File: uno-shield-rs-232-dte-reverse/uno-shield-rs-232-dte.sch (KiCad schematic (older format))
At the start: 19 parts, among them J1 Ctrl Route, J3 DSR/CTS, J4 DB9_Male, P1 Power, P2 Analog, P3 Digital, P4 Digital, P5 CONN_01X01, P7 CONN_01X01, U1 MAX232

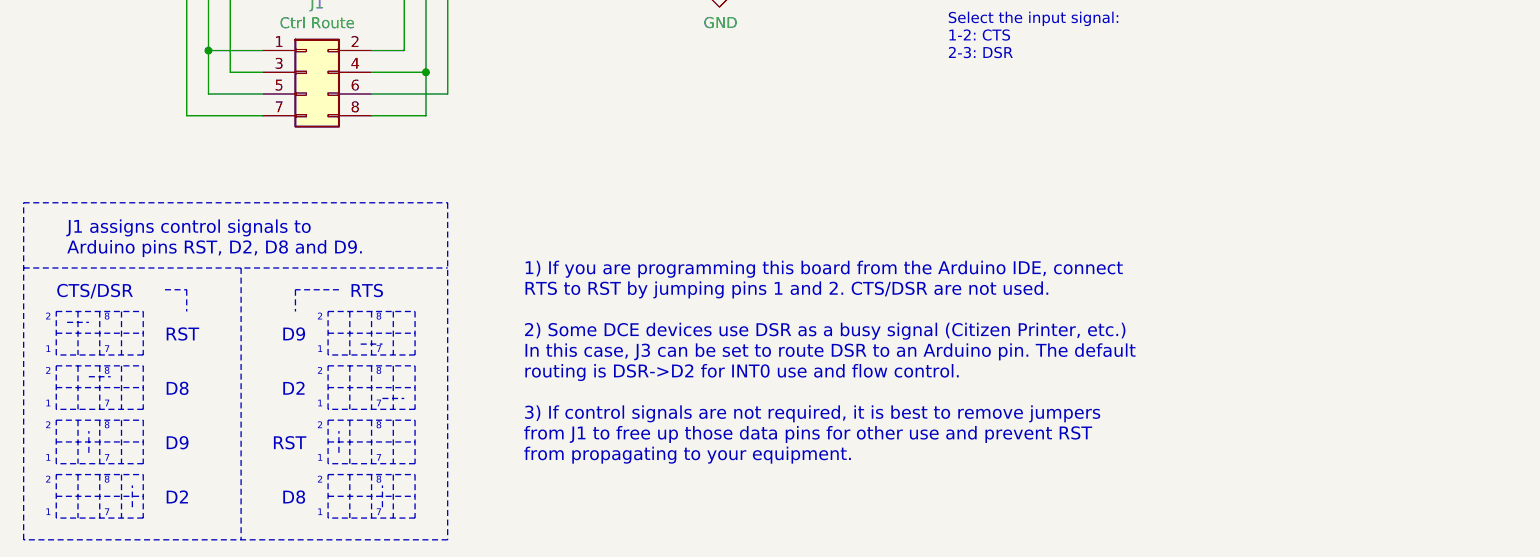
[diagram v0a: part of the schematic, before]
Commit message: Add DTE-Reverse
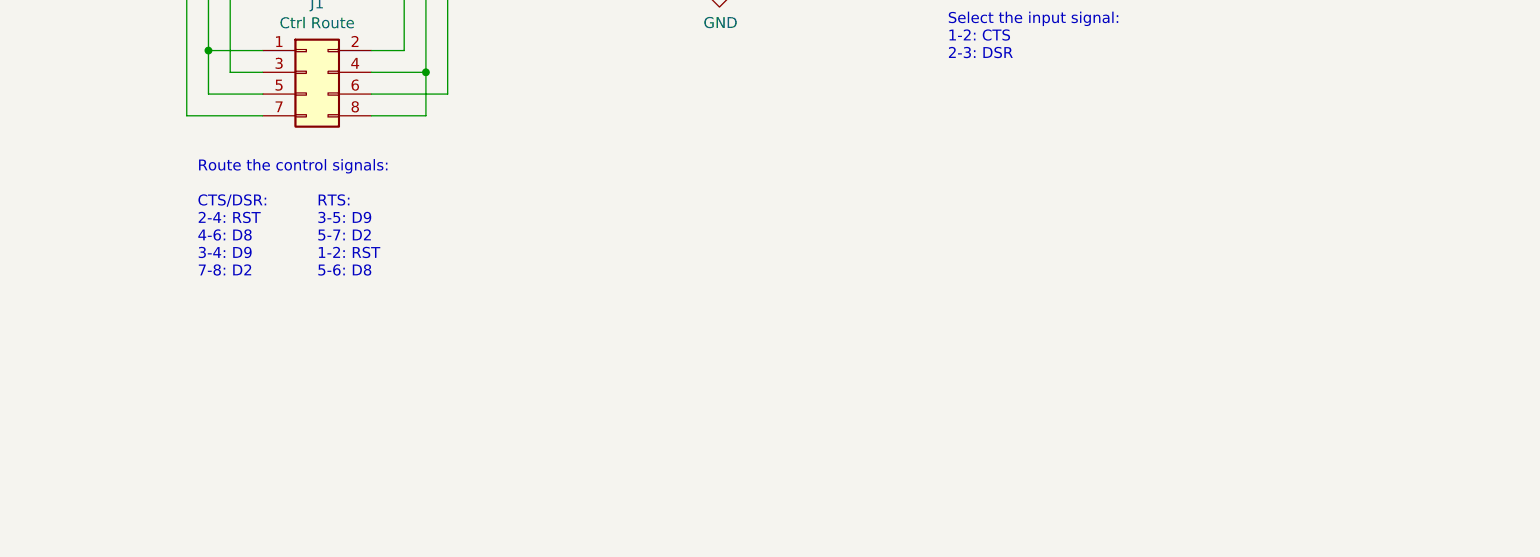
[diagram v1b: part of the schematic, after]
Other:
- note added: "RTS:\n3-5: D9\n5-7: D2\n1-2: RST\n5-6: D8"
- note added: "Route the control signals:\n\nCTS/DSR:\n2-4: RST\n4-6: D8\n3-4: D9\n7-8: D2"
- note removed: "1) If you are programming this board from the Arduino IDE, connect\nRTS to RST by jumping pins 1 and 2. CTS/DSR are not used.\n\n2) Some DCE devices use DSR as a busy signal (Citizen Printer, etc.)\nIn this case, J3 can be set to route DSR to an Arduino pin. The default\nrouting is DSR->D2 for INT0 use and flow control.\n\n3) If control signals are not required, it is best to remove jumpers\nfrom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"
- note removed: "2 8\n\n\n1 7"
- note removed: "CTS/DSR"
- note removed: "D2"
- note removed: "D8"
- note removed: "D9"
- note removed: "J1 assigns control signals to\nArduino pins RST, D2, D8 and D9."
- note removed: "RST"
- note removed: "RTS"
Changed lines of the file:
@@
 EESchema Schematic File Version 4
-LIBS:uno-shield-rs-232-dte-cache
+LIBS:uno-shield-rs-232-dce-cache
 EELAYER 30 0
 EELAYER END
@@
 NoConn ~ 9450 2700
 NoConn ~ 9450 2800
-Wire Notes Line
-	1100 5100 1500 5100
-Wire Notes Line
-	1500 5100 1500 5300
-Wire Notes Line
-	1500 5300 1100 5300
-Wire Notes Line
-	1100 5300 1100 5100
-Wire Notes Line
-	1200 5100 1200 5300
-Wire Notes Line
-	1300 5100 1300 5300
-Wire Notes Line
-	1400 5100 1400 5300
-Wire Notes Line
-	1100 5200 1500 5200
-Wire Notes Line
-	1100 5350 1500 5350
-Wire Notes Line
-	1500 5350 1500 5550
-Wire Notes Line
-	1500 5550 1100 5550
-Wire Notes Line
-	1100 5550 1100 5350
-Wire Notes Line
-	1200 5350 1200 5550
-Wire Notes Line
-	1300 5350 1300 5550
-Wire Notes Line
-	1400 5350 1400 5550
-Wire Notes Line
-	1100 5450 1500 5450
-Wire Notes Line
-	1100 5600 1500 5600
-Wire Notes Line
-	1500 5600 1500 5800
-Wire Notes Line
-	1500 5800 1100 5800
-Wire Notes Line
-	1100 5800 1100 5600
-Wire Notes Line
-	1200 5600 1200 5800
-Wire Notes Line
-	1300 5600 1300 5800
-Wire Notes Line
-	1400 5600 1400 5800
-Wire Notes Line
-	1100 5700 1500 5700
-Wire Notes Line
-	1100 5850 1500 5850
-Wire Notes Line
-	1500 5850 1500 6050
-Wire Notes Line
-	1500 6050 1100 6050
-Wire Notes Line
-	1100 6050 1100 5850
-Wire Notes Line
-	1200 5850 1200 6050
-Wire Notes Line
-	1300 5850 1300 6050
-Wire Notes Line
-	1400 5850 1400 6050
-Wire Notes Line
-	1100 5950 1500 5950
-Wire Notes Line
-	2350 5100 2750 5100
-Wire Notes Line
-	2750 5100 2750 5300
-Wire Notes Line
-	2750 5300 2350 5300
-Wire Notes Line
-	2350 5300 2350 5100
-Wire Notes Line
-	2450 5100 2450 5300
-Wire Notes Line
-	2550 5100 2550 5300
-Wire Notes Line
-	2650 5100 2650 5300
-Wire Notes Line
-	2350 5200 2750 5200
-Wire Notes Line
-	2350 5350 2750 5350
-Wire Notes Line
-	2750 5350 2750 5550
-Wire Notes Line
-	2750 5550 2350 5550
-Wire Notes Line
-	2350 5550 2350 5350
-Wire Notes Line
-	2450 5350 2450 5550
-Wire Notes Line
-	2550 5350 2550 5550
-Wire Notes Line
-	2650 5350 2650 5550
-Wire Notes Line
-	2350 5450 2750 5450
-Wire Notes Line
-	2350 5600 2750 5600
-Wire Notes Line
-	2750 5600 2750 5800
-Wire Notes Line
-	2750 5800 2350 5800
-Wire Notes Line
-	2350 5800 2350 5600
-Wire Notes Line
-	2450 5600 2450 5800
-Wire Notes Line
-	2550 5600 2550 5800
-Wire Notes Line
-	2650 5600 2650 5800
-Wire Notes Line
-	2350 5700 2750 5700
-Wire Notes Line
-	2350 5850 2750 5850
-Wire Notes Line
-	2750 5850 2750 6050
-Wire Notes Line
-	2750 6050 2350 6050
-Wire Notes Line
-	2350 6050 2350 5850
-Wire Notes Line
-	2450 5850 2450 6050
-Wire Notes Line
-	2550 5850 2550 6050
-Wire Notes Line
-	2650 5850 2650 6050
-Wire Notes Line
-	2350 5950 2750 5950
-Wire Notes Line width 100
-	1150 5150 1250 5150
-Wire Notes Line width 100
-	1250 5400 1350 5400
-Wire Notes Line width 100
-	1250 5750 1250 5650
-Wire Notes Line width 100
-	1450 6000 1450 5900
-Wire Notes Line width 100
-	2500 5250 2600 5250
-Wire Notes Line width 100
-	2600 5500 2700 5500
-Wire Notes Line width 100 style solid
-	2400 5750 2400 5650
-Wire Notes Line width 100
-	2600 6000 2600 5900
-Text Notes 1050 5300 0    31   ~ 0
-2                  8\n\n\n1                  7
-Text Notes 1050 5550 0    31   ~ 0
-2                  8\n\n\n1                  7
-Text Notes 1050 5800 0    31   ~ 0
-2                  8\n\n\n1                  7
-Text Notes 1050 6050 0    31   ~ 0
-2                  8\n\n\n1                  7
-Text Notes 2300 5300 0    31   ~ 0
-2                  8\n\n\n1                  7
-Text Notes 2300 5550 0    31   ~ 0
-2                  8\n\n\n1                  7
-Text Notes 2300 5800 0    31   ~ 0
-2                  8\n\n\n1                  7
-Text Notes 2300 6050 0    31   ~ 0
-2                  8\n\n\n1                  7
-Text Notes 1150 4850 0    59   ~ 0
-J1 assigns control signals to\nArduino pins RST, D2, D8 and D9.
-Text Notes 1100 5050 0    59   ~ 0
-CTS/DSR
-Text Notes 2450 5050 0    59   ~ 0
-RTS
-Text Notes 1600 5250 0    59   ~ 0
-RST
-Text Notes 1600 5500 0    59   ~ 0
-D8
-Text Notes 1600 5750 0    59   ~ 0
-D9
-Text Notes 1600 6000 0    59   ~ 0
-D2
-Text Notes 2250 5250 2    59   ~ 0
-D9
-Text Notes 2250 5500 2    59   ~ 0
-D2
-Text Notes 2250 5750 2    59   ~ 0
-RST
-Text Notes 2250 6000 2    59   ~ 0
-D8
-Wire Notes Line
-	950  4900 2900 4900
-Wire Notes Line
-	2900 6150 950  6150
-Wire Notes Line
-	950  6150 950  4600
-Wire Notes Line
-	950  4600 2900 4600
-Wire Notes Line
-	2900 4600 2900 6150
-Wire Notes Line
-	1950 4900 1950 6150
-Wire Notes Line
-	1600 5000 1700 5000
-Wire Notes Line
-	1700 5000 1700 5100
-Wire Notes Line
-	2400 5000 2200 5000
-Wire Notes Line
-	2200 5000 2200 5100
-Text Notes 3250 5800 0    59   ~ 0
-1) If you are programming this board from the Arduino IDE, connect\nRTS to RST by jumping pins 1 and 2. CTS/DSR are not used.\n\n2) Some DCE devices use DSR as a busy signal (Citizen Printer, etc.)\nIn this case, J3 can be set to route DSR to an Arduino pin. The default\nrouting is DSR->D2 for INT0 use and flow control.\n\n3) If control signals are not required, it is best to remove jumpers\nfrom J1 to free up those data pins for other use and prevent RST\nfrom propagating to your equipment.
+Text Notes 1750 4950 0    50   ~ 0
+Route the control signals:\n\nCTS/DSR:\n2-4: RST\n4-6: D8\n3-4: D9\n7-8: D2
+Text Notes 2300 4950 0    50   ~ 0
+RTS:\n3-5: D9\n5-7: D2\n1-2: RST\n5-6: D8
 $EndSCHEMATC

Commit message: Propagate signal routing changes to DTE-R shield.
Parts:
- added J2: RX Route, Connector_PinHeader_2.54mm:PinHeader_2x05_P2.54mm_Vertical, symbol Connector_Generic:Conn_02x05_Odd_Even
- added J5: TX Route, Connector_PinHeader_2.54mm:PinHeader_1x05_P2.54mm_Vertical, symbol Connector_Generic:Conn_01x05
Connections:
- net labels added: D3, D4, URX, UTX
- net labels removed: 3(**), 4
- wire segments 108 -> 114
- no-connect marks 24 -> 26
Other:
- note added: "1 3"
- note added: "1) If you are programming this board from the Arduino IDE, connect\nRTS to RST by jumping pins 1 and 2. CTS/DSR are not used.\n\n2) Some DCE devices use DSR as a busy signal (Citizen Printer, etc.)\nIn this case, J3 can be set to route DSR to an Arduino pin. The default\nrouting is DSR->D2 for INT0 use and flow control.\n\n3) If control signals are not required, it is best to remove jumpers\nfrom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"
- note added: "2 8\n\n\n1 7"
- note added: "CTS/DSR"
- note added: "D2"
- note added: "D8"
- note added: "D9"
- note added: "Default Serial:\nRX -> RX,\nTX -> TX"
- note added: "J1 assigns control signals to\nArduino pins RST, D2, D8 and D9."
- note added: "RST"
- note added: "RTS"
- note added: "Software Serial, with\nD2 open for INT0:\nRX -> D3\nTX -> D4"
- note added: "Software Serial, with\nD3 open for PWM:\nRX -> D2\nTX -> D4"
- note added: "Software Serial:\nRX -> D2,\nTX -> D3"
- note removed: "RTS:\n3-5: D9\n5-7: D2\n1-2: RST\n5-6: D8"
- note removed: "Route the control signals:\n\nCTS/DSR:\n2-4: RST\n4-6: D8\n3-4: D9\n7-8: D2"
